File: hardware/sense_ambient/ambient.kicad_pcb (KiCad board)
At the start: 2 copper layers, 12.5 x 11 mm, 9 parts, among them J1 MOLEX_SlimStack_505551-1020, SW1 ReedSW_NO, U1 OPT3002DNPR, U2 HDC2010YPAR

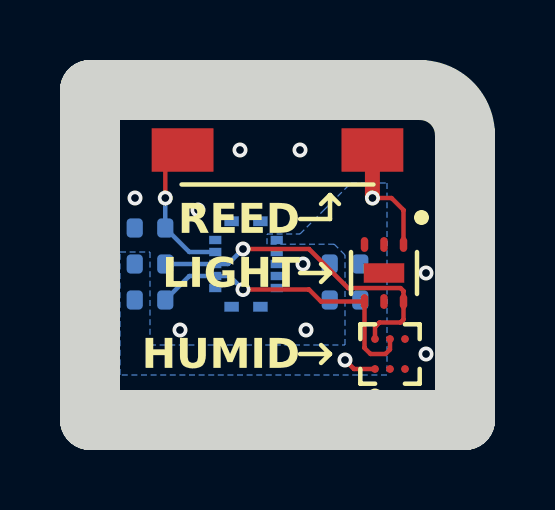
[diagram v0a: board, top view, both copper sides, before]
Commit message: corrected pin mating to sensor module
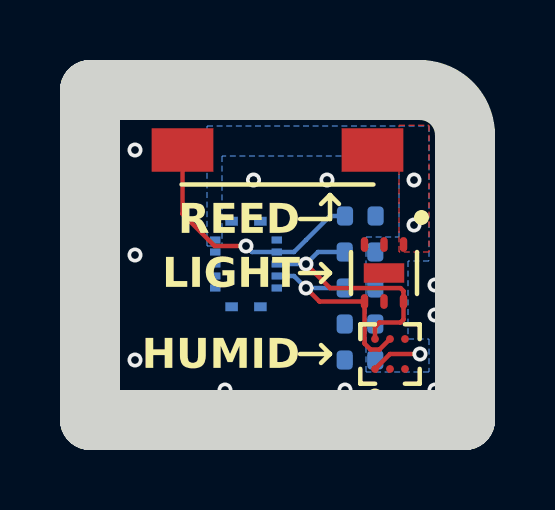
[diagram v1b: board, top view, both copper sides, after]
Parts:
- moved R3 7.02 mm to (109.0, 54.2), turned to 0 degrees
- moved R1 7.01 mm to (109.0, 56.6), turned to 180 degrees
- moved R2 7.01 mm to (109.0, 55.4), turned to 180 degrees
- moved C1 2.06 mm to (109.0, 59.0)
- moved C2 2.06 mm to (109.0, 57.8)
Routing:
- net /REED: track 4.60 -> 8.57 mm
- net +3V3: track 5.07 -> 1.71 mm, vias 2 -> 3
- net /SCL: track 10.2 -> 7.04 mm
- net /SDA: track 11.1 -> 8.46 mm
- net GND: vias 9 -> 10
- added copper zone on F.Cu, net +3V3
